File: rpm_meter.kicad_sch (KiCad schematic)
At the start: 0 parts

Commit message: Shifting registers
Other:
- removed sheet led_segment0
- removed sheet led_segment1
- removed sheet led_segment2
- removed sheet led_segment3
- removed sheet led_segment4
- removed sheet led_segment5
- removed sheet led_segment6
- removed sheet led_segment7
- removed sheet led_segment8
- removed sheet led_segment9
- added sheet Leds (leds.kicad_sch)
- sheet mcu ports: added none; removed green_led_0, green_led_1, green_led_2, green_led_3, green_led_4, green_led_5, green_led_6, green_led_7, green_led_8, green_led_9, red_led_0, red_led_1, red_led_2, red_led_3, red_led_4, red_led_5, red_led_6, red_led_7, red_led_8, red_led_9

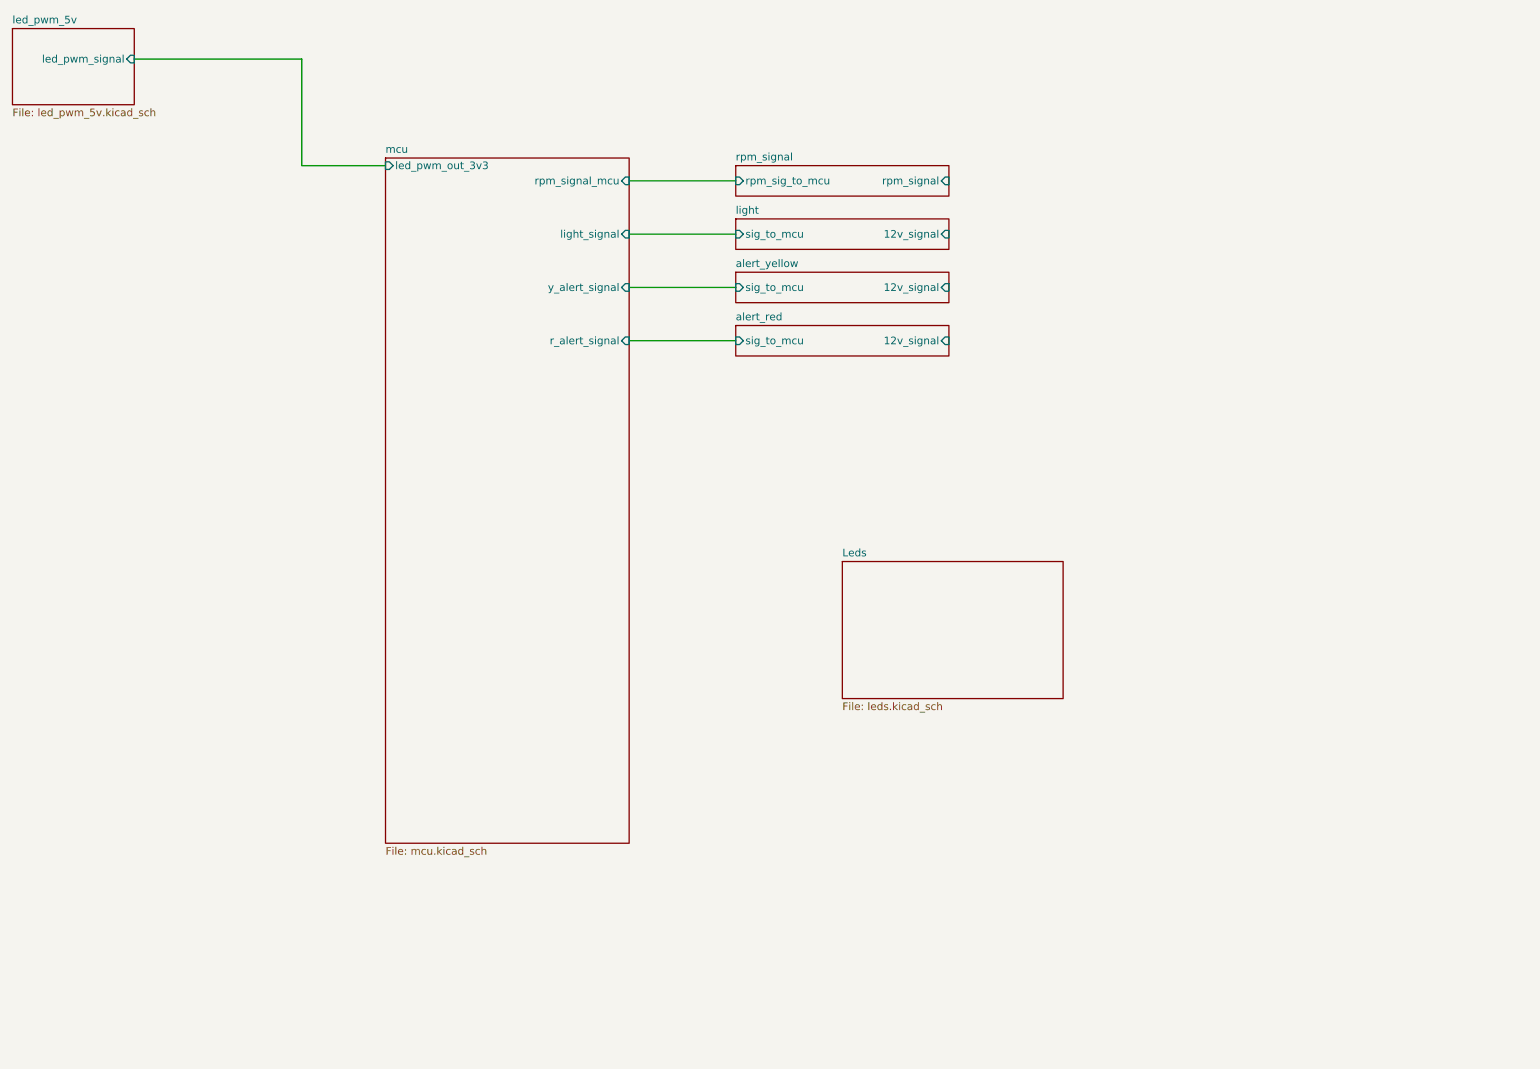
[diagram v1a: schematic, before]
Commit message: Step_down 5v
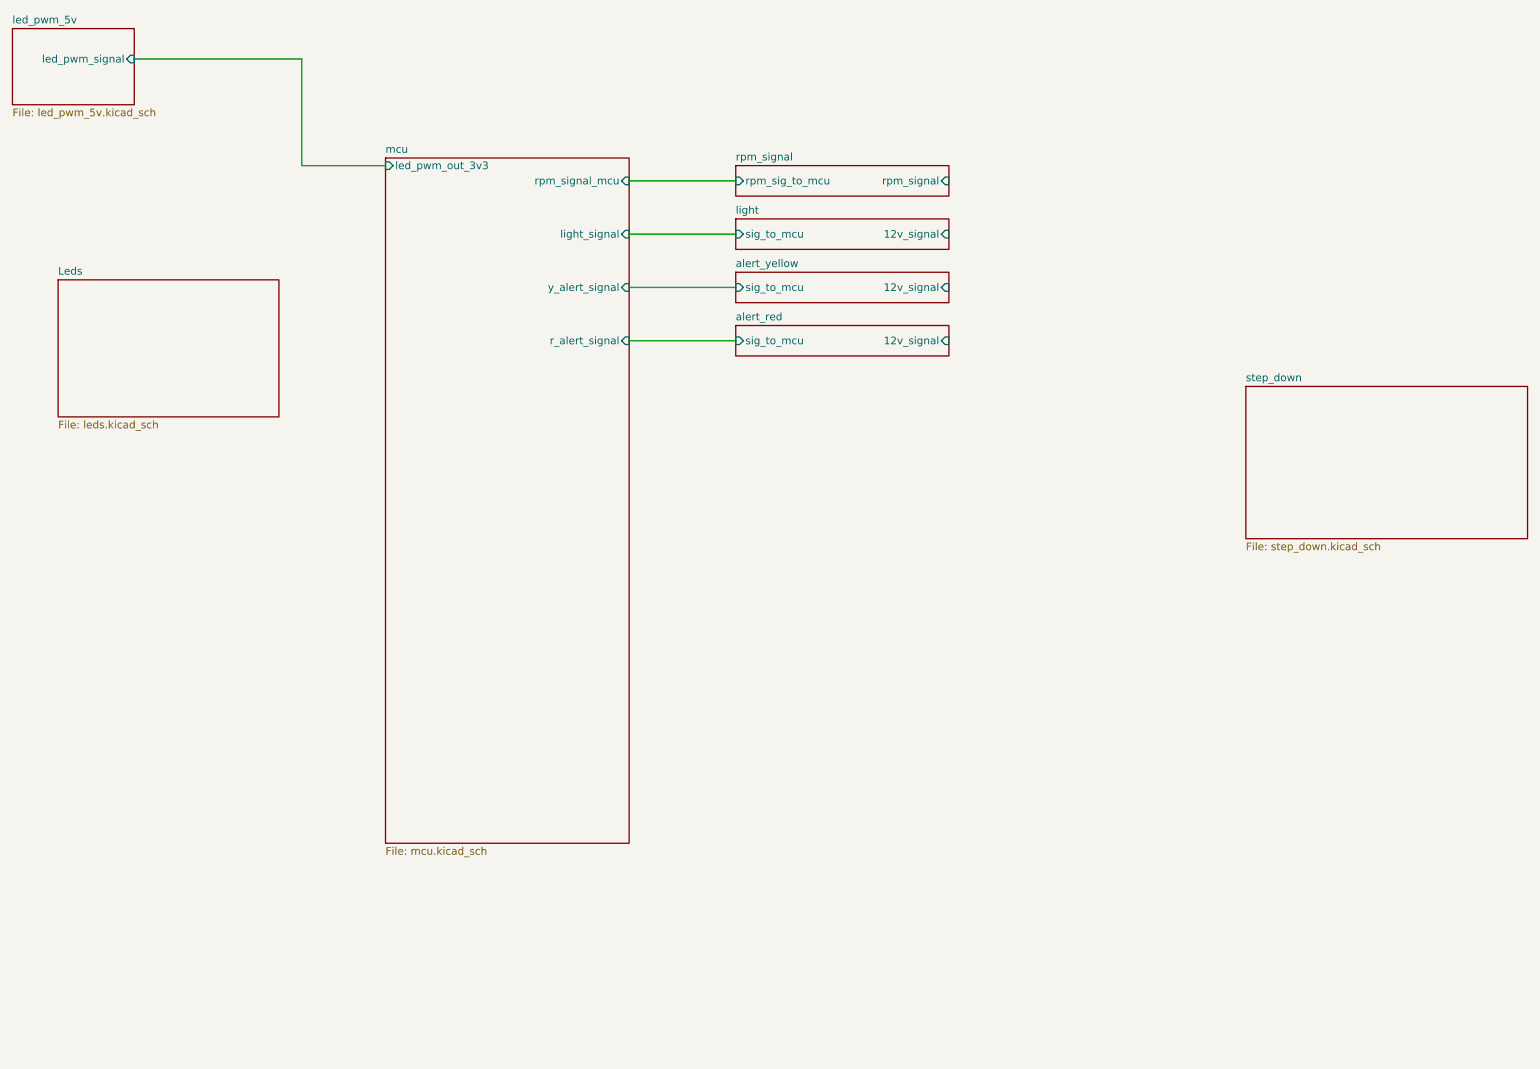
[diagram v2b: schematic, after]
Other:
- added sheet step_down (step_down.kicad_sch)
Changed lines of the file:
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@@
 	)
 	(sheet
-		(at 156.21 106.68)
+		(at 25.4 59.69)
 		(size 36.83 22.86)
 		(fields_autoplaced yes)
@@
 		)
 		(property "Sheetname" "Leds"
-			(at 156.21 105.9684 0)
+			(at 25.4 58.9784 0)
 			(effects
 				(font
@@
 		)
 		(property "Sheetfile" "leds.kicad_sch"
-			(at 156.21 130.1246 0)
+			(at 25.4 83.1346 0)
 			(effects
 				(font
@@
 				)
 			)
+		)
+	)
+	(sheet
+		(at 223.52 77.47)
+		(size 46.99 25.4)
+		(fields_autoplaced yes)
+		(stroke
+			(width 0.1524)
+			(type solid)
+		)
+		(fill
+			(color 0 0 0 0.0000)
+		)
+		(property "Sheetname" "step_down"
+			(at 223.52 76.7584 0)
+			(effects
+				(font
+					(size 1.27 1.27)
+				)
+				(justify left bottom)
+			)
+		)
+		(property "Sheetfile" "step_down.kicad_sch"
+			(at 223.52 103.4546 0)
+			(effects
+				(font
+					(size 1.27 1.27)
+				)
+				(justify left top)
+			)
+		)
+		(instances
+			(project "rpm_meter"
+				(path "/c95b12ac-441d-4f7a-bd6a-c2e5d81eb286"
+					(page "29")
+				)
+			)

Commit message: New template
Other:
- company: (none) -> STAPsystem
- title: (none) -> RPM meter LED
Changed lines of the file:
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@@
 	(generator_version "8.0")
 	(paper "A4")
+	(title_block
+		(title "RPM meter LED")
+		(date "2024-11-26")
+		(rev "v1.0")
+		(company "STAPsystem")
+		(comment 1 "Adrian Pietrzak")
+	)
 	(wire
 		(pts

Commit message: 27112024
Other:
- sheet Leds ports: added Clock_spi, LATCH, MOSI; removed none
- sheet mcu ports: added LATCH_PIN, SPI_MOSI, SPI_SCK; removed none
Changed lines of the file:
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@@
+	(wire
+		(pts
+			(xy 62.23 67.31) (xy 80.01 67.31)
+		)
+		(stroke
+			(width 0)
+			(type default)
+		)
+	)
 	(wire
 		(pts
@@
 		(pts
 			(xy 66.04 22.86) (xy 38.1 22.86)
+		)
+		(stroke
+			(width 0)
+			(type default)
+		)
+	)
+	(wire
+		(pts
+			(xy 62.23 62.23) (xy 80.01 62.23)
+		)
+		(stroke
+			(width 0)
+			(type default)
+		)
+	)
+	(wire
+		(pts
+			(xy 62.23 64.77) (xy 80.01 64.77)
 		)
 		(stroke
@@
 			)
 		)
+		(pin "SPI_MOSI" input
+			(at 80.01 62.23 180)
+			(effects
+				(font
+					(size 1.27 1.27)
+				)
+				(justify left)
+			)
+		)
+		(pin "SPI_SCK" input
+			(at 80.01 64.77 180)
+			(effects
+				(font
+					(size 1.27 1.27)
+				)
+				(justify left)
+			)
+		)
+		(pin "LATCH_PIN" input
+			(at 80.01 67.31 180)
+			(effects
+				(font
+					(size 1.27 1.27)
+				)
+				(justify left)
+			)
+		)
 		(instances
 			(project "rpm_meter"
@@
 	)
 	(sheet
-		(at 25.4 59.69)
-		(size 36.83 22.86)
+		(at 46.99 59.69)
+		(size 15.24 10.16)
 		(fields_autoplaced yes)
 		(stroke
@@
 		)
 		(property "Sheetname" "Leds"
-			(at 25.4 58.9784 0)
+			(at 46.99 58.9784 0)
 			(effects
 				(font
@@
 		)
 		(property "Sheetfile" "leds.kicad_sch"
-			(at 25.4 83.1346 0)
+			(at 46.99 70.4346 0)
 			(effects
 				(font
@@
 			)
 		)
+		(pin "MOSI" input
+			(at 62.23 62.23 0)
+			(effects
+				(font
+					(size 1.27 1.27)
+				)
+				(justify right)
+			)
+		)
+		(pin "Clock_spi" input
+			(at 62.23 64.77 0)
+			(effects
+				(font
+					(size 1.27 1.27)
+				)
+				(justify right)
+			)
+		)
+		(pin "LATCH" input
+			(at 62.23 67.31 0)
+			(effects
+				(font
+					(size 1.27 1.27)
+				)
+				(justify right)
+			)
+		)

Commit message: ws2812b
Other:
- sheet Leds ports: added WS2812B_IN; removed Clock_spi, LATCH, MOSI
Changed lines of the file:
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@@
-	(wire
-		(pts
-			(xy 62.23 67.31) (xy 80.01 67.31)
-		)
-		(stroke
-			(width 0)
-			(type default)
-		)
-	)
 	(wire
 		(pts
@@
 		(pts
 			(xy 66.04 22.86) (xy 38.1 22.86)
-		)
-		(stroke
-			(width 0)
-			(type default)
-		)
-	)
-	(wire
-		(pts
-			(xy 62.23 62.23) (xy 80.01 62.23)
-		)
-		(stroke
-			(width 0)
-			(type default)
-		)
-	)
-	(wire
-		(pts
-			(xy 62.23 64.77) (xy 80.01 64.77)
 		)
 		(stroke
@@
 	)
 	(sheet
-		(at 46.99 59.69)
-		(size 15.24 10.16)
+		(at 49.53 62.23)
+		(size 15.24 5.08)
 		(fields_autoplaced yes)
 		(stroke
@@
 		)
 		(property "Sheetname" "Leds"
-			(at 46.99 58.9784 0)
+			(at 49.53 61.5184 0)
 			(effects
 				(font
@@
 		)
 		(property "Sheetfile" "leds.kicad_sch"
-			(at 46.99 70.4346 0)
-			(effects
-				(font
-					(size 1.27 1.27)
-				)
-				(justify left top)
-			)
-		)
-		(pin "MOSI" input
-			(at 62.23 62.23 0)
-			(effects
-				(font
-					(size 1.27 1.27)
-				)
-				(justify right)
-			)
-		)
-		(pin "Clock_spi" input
-			(at 62.23 64.77 0)
-			(effects
-				(font
-					(size 1.27 1.27)
-				)
-				(justify right)
-			)
-		)
-		(pin "LATCH" input
-			(at 62.23 67.31 0)
-			(effects
-				(font
+			(at 49.53 67.8946 0)
+			(effects
+				(font
+					(size 1.27 1.27)
+				)
+				(justify left top)
+			)
+		)
+		(pin "WS2812B_IN" input
+			(at 64.77 64.77 0)
+			(effects
+				(font

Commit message: Placed footprints v1.0
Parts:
- added J1, J3, J4, J5, J6, J7: Conn_01x01_Socket, Connector_Wire:SolderWire-0.15sqmm_1x01_D0.5mm_OD1.5mm, symbol Connector:Conn_01x01_Socket
- added U5: PEC11R-4225F-S0024, Library_local:PEC12R-4XXXF-SXXXX_1, symbol local_library:PEC11R-4225F-S0024
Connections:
- net alert_red/12v_signal: now also J7.1 (Pin_1)
- net alert_yellow/12v_signal: now also J6.1 (Pin_1)
- net light/12v_signal: now also J5.1 (Pin_1)
- net rpm_signal/rpm_signal: now also J4.1 (Pin_1)
- new net +12V: J1.1 (Pin_1)
- new net GND: J3.1 (Pin_1)
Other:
- removed sheet led_pwm_5v

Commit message: Encoder
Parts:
- removed U5: PEC11R-4225F-S0024, Library_local:PEC12R-4XXXF-SXXXX_1, symbol local_library:PEC11R-4225F-S0024
- added C18, C19, C20: 100n, Capacitor_SMD:C_0603_1608Metric, symbol Device:C_Small
- added R10, R11, R8: 10k, Resistor_SMD:R_0603_1608Metric, symbol Device:R
- added R12, R13, R16: 1k, Resistor_SMD:R_0603_1608Metric, symbol Device:R
- added SW1: RotaryEncoder_Switch_MP, Library_local:RotaryEncoder_Alps_EC12E-Switch_Vertical_H20mm, symbol Device:RotaryEncoder_Switch_MP
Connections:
- net GND: now also C18.1, C19.1, C20.1, SW1.C, SW1.S2
- new net: R11.1, R16.1, SW1.S1
- new net: R12.1, R8.1, SW1.A
- new net: R10.1, R13.1, SW1.B
- new net +3.3V: R10.2, R11.2, R8.2
- new net mcu/ENCODER_A: C20.2, R12.2
- new net mcu/ENCODER_B: C19.2, R13.2
- new net mcu/ENCODER_BTN: C18.2, R16.2
- no-connect marks 0 -> 1
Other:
- sheet mcu ports: added ENCODER_A, ENCODER_B, ENCODER_BTN; removed none
